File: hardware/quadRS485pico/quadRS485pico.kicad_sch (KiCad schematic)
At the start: 23 parts, among them IC1 THVD2450DRBR, IC2 THVD2450DRBR, IC3 THVD2450DRBR, IC4 THVD2450DRBR, J1 Conn_01x02_Pin, J2 Conn_01x02_Pin, J3 Conn_01x02_Pin, J4 Conn_01x02_Pin, J7 Conn_01x06, Q1 DMG2301L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

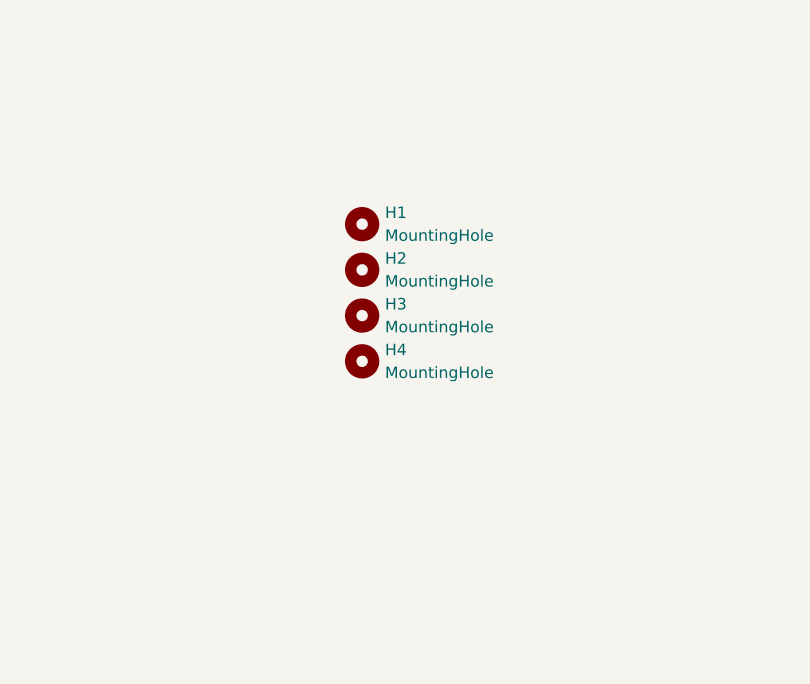
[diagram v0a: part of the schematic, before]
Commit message: add pinout info, add vias, make it double side, clean the board
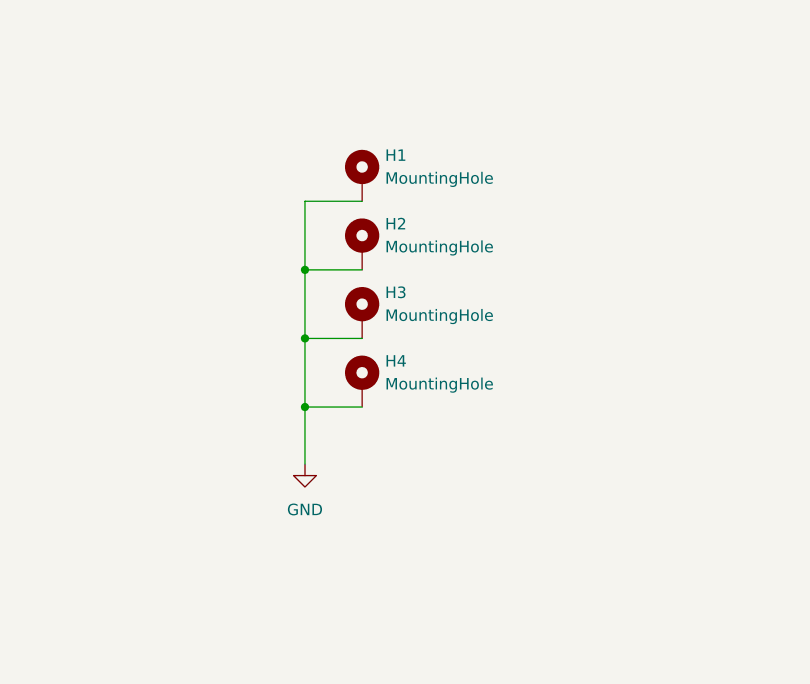
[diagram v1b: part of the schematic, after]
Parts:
- H1: symbol Mechanical:MountingHole -> Mechanical:MountingHole_Pad; now left out of the parts list
- H2, H3, H4: footprint MountingHole:MountingHole_2.5mm_Pad_TopOnly -> MountingHole:MountingHole_2.5mm_Pad_TopBottom; symbol Mechanical:MountingHole -> Mechanical:MountingHole_Pad; now left out of the parts list
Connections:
- net GND: now also H1.1, H2.1, H3.1, H4.1
